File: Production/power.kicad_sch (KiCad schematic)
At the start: 10 parts, among them U204 TPS62177DQCR

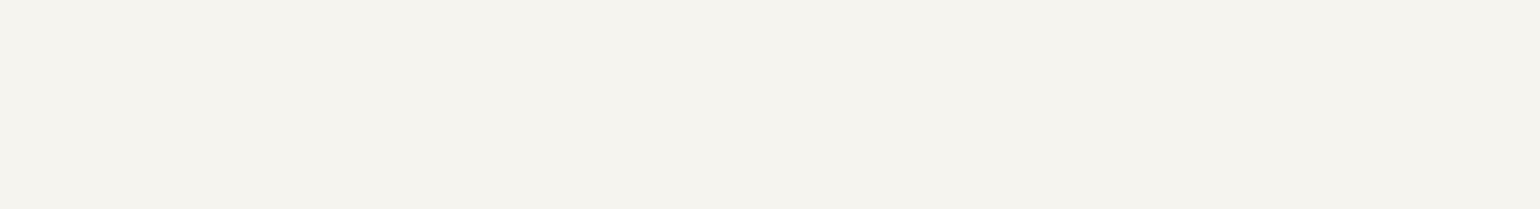
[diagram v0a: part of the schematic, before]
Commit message: Production: four SMT cover standoffs H101-H104, no screw holes
The board has no screw holes (cover screws go into the tray pillars beside
the corner notches). Adds the four F.Cu cover standoffs the mechanical model
already called for: Wurth WA-SMSI 9774035243R (M2 x 3.5 mm, LCSC C5266183),
no net, on the 3V3 Rail sheet. The upper pair moves from tray z 56 to z 48
(it sat on the port-1 BQ25756 and the BLE module end); a new mechanical check
keeps them >= 5 mm from the module. make_board.py --standoffs places and
locks them after Update PCB from Schematic.

Co-Authored-By: Claude Opus 5.5 <noreply@anthropic.com>
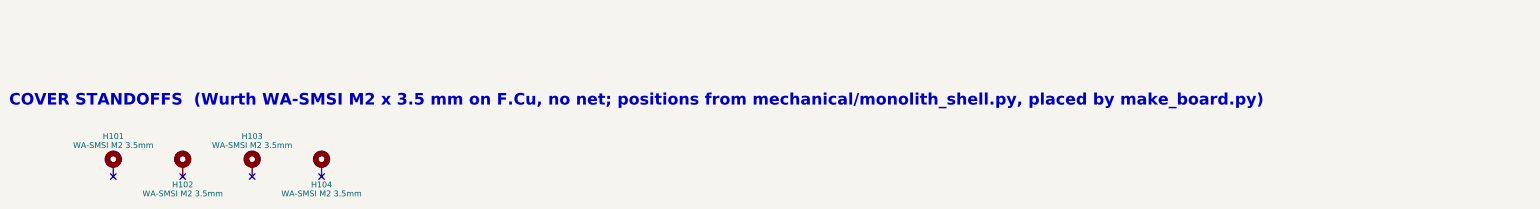
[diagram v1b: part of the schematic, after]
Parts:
- added H101, H102, H103, H104: WA-SMSI M2 3.5mm, Mounting_Wuerth:Mounting_Wuerth_WA-SMSI-M2_H3.5mm_9774035243, symbol Mechanical:MountingHole_Pad
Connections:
- no-connect marks 1 -> 5
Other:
- note added: "COVER STANDOFFS (Wurth WA-SMSI M2 x 3.5 mm on F.Cu, no net; positions from mechanical/monolith_shell.py, placed by make_board.py)"
